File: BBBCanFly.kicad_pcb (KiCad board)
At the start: 2 copper layers, 86.4 x 54.7 mm, 26 parts, among them P1 CONN_01X02, P12 CONN_01X03, P13 CONN_01X03, P2 CONN_1x2, P3 CONN_02X23, P4 CONN_02X23, P5 CONN_02X05, P6 CONN_10, P7 CONN_4, P8 CONN_01X03, P9 CONN_01X03, U1 HT7465

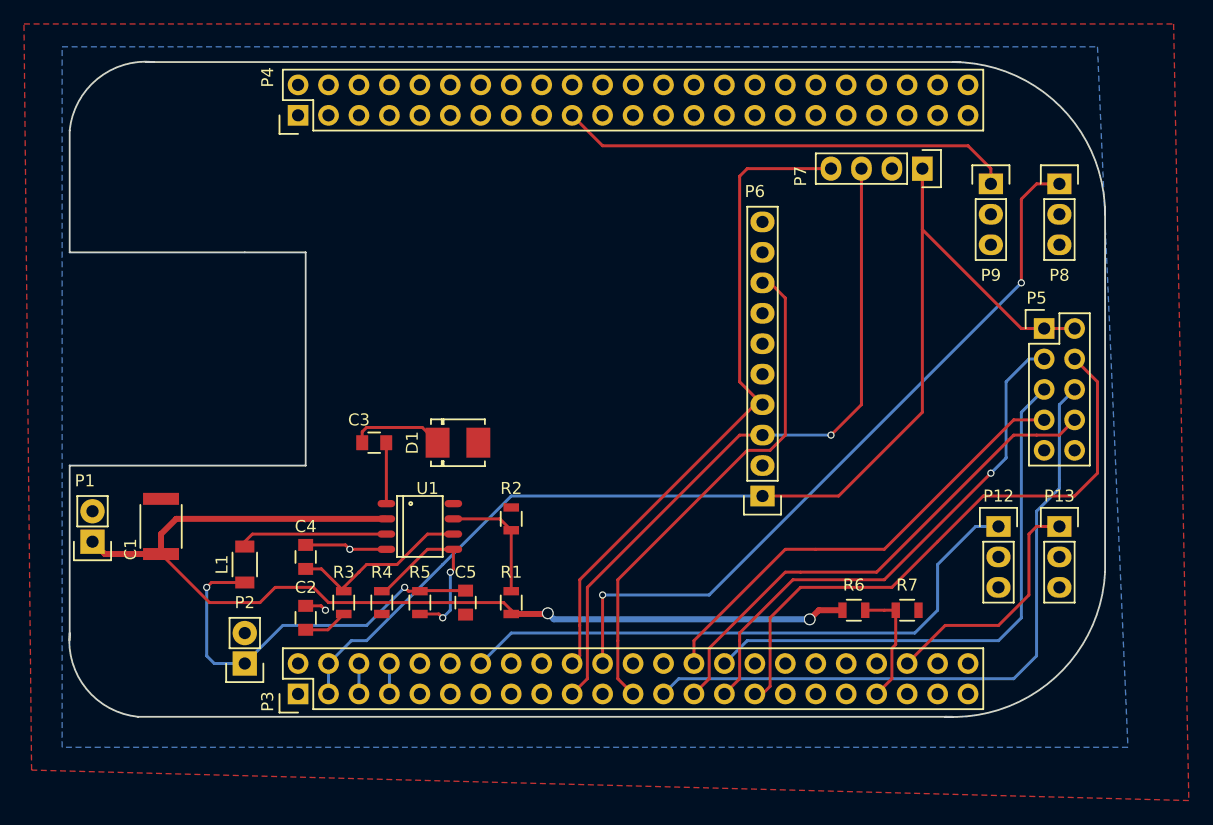
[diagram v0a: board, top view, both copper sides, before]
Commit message: modified power supply program
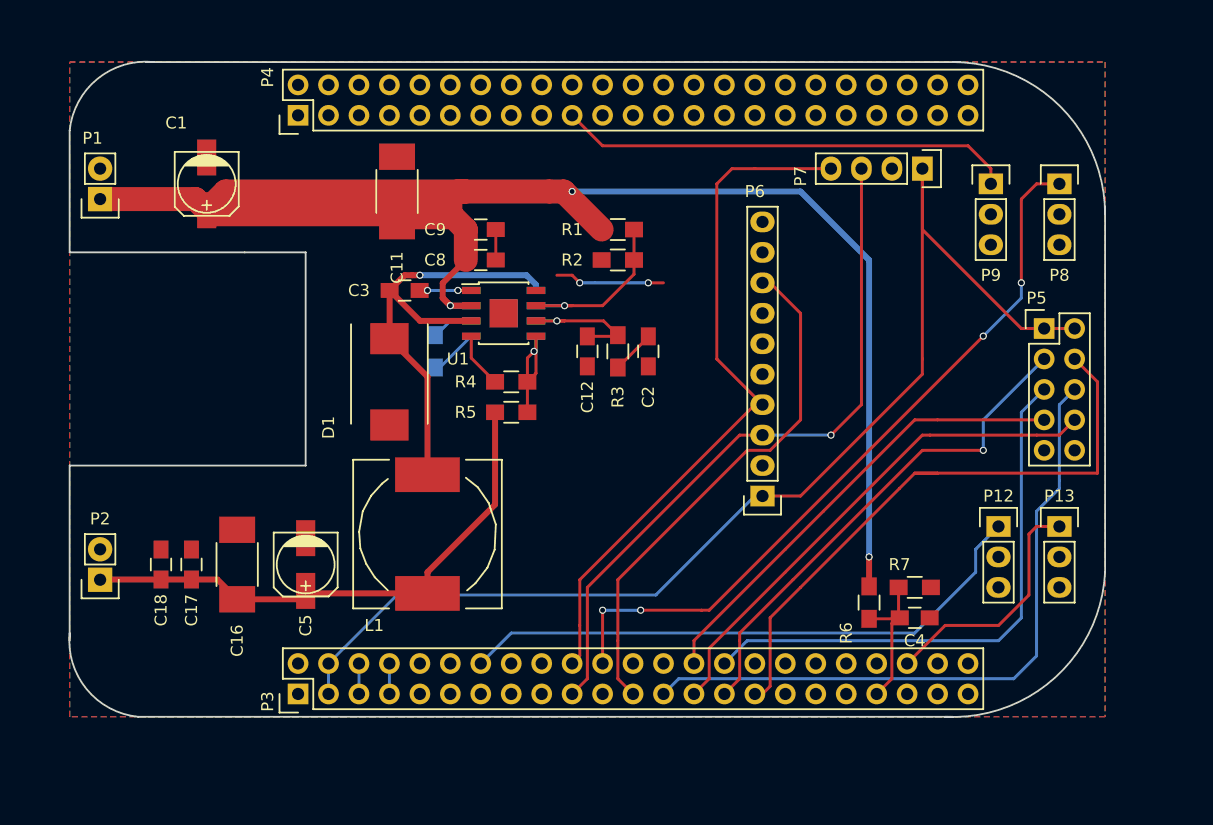
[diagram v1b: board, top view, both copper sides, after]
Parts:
- added C11: C, Capacitors_SMD:C_1812_HandSoldering, F.Cu at (52.7, 36.2)
- added C12: C, Capacitors_SMD:C_0805_HandSoldering, F.Cu at (68.6, 49.5)
- added C16: C, Capacitors_SMD:C_1812_HandSoldering, F.Cu at (39.4, 67.3)
- added C17: C, Capacitors_SMD:C_0805_HandSoldering, F.Cu at (35.6, 67.3)
- added C18: C, Capacitors_SMD:C_0805_HandSoldering, F.Cu at (33.0, 67.3)
- added C8: C, Capacitors_SMD:C_0805_HandSoldering, F.Cu at (59.7, 41.9)
- added C9: C, Capacitors_SMD:C_0805_HandSoldering, F.Cu at (59.7, 39.4)
- added R8: 200k, Resistors_SMD:R_0805_HandSoldering, B.Cu at (55.9, 49.5)
- added U2: MP1584EN, Housings_SOIC:SOIC-8-1EP_3.9x4.9mm_Pitch1.27mm, B.Cu at (61.6, 46.4)
- C1: footprint Capacitors_SMD:C_1812 -> Capacitors_SMD:c_elec_5x5.7
- C2, C3: footprint Capacitors_SMD:C_0805 -> Capacitors_SMD:C_0805_HandSoldering
- C4: value 1n -> 10p; footprint Capacitors_SMD:C_0805 -> Capacitors_SMD:C_0805_HandSoldering
- C5: footprint Capacitors_SMD:C_0805 -> Capacitors_SMD:c_elec_5x5.7
- D1: footprint Diodes_SMD:DO-214BA -> Diodes_SMD:DO-214AB
- L1: footprint Capacitors_SMD:C_1206 -> Inductors_NEOSID:Neosid_Inductor_SM-NE127
- R1: value 10k -> 100k; footprint Resistors_SMD:R_0805 -> Resistors_SMD:R_0805_HandSoldering
- R2, R3, R4, R6, R7: footprint Resistors_SMD:R_0805 -> Resistors_SMD:R_0805_HandSoldering
- R5: value 44.2k -> 47k; footprint Resistors_SMD:R_0805 -> Resistors_SMD:R_0805_HandSoldering
- U1: footprint Power_Integrations:SO-8 -> Housings_SOIC:SOIC-8-1EP_3.9x4.9mm_Pitch1.27mm
- moved C4 51.1 mm to (95.9, 71.8), turned to 0 degrees
- moved C2 36.2 mm to (73.7, 49.5), turned to 270 degrees
- moved R1 32.4 mm to (71.1, 39.4), turned to 0 degrees
- moved R3 31.0 mm to (71.1, 49.5)
- moved C1 28.8 mm to (36.8, 35.6), turned to 270 degrees
- moved P1 28.6 mm to (27.9, 36.8)
- moved R2 23.3 mm to (71.1, 41.9), turned to 180 degrees
- moved R4 21.3 mm to (62.2, 52.1), turned to 180 degrees
- moved U1 19.1 mm to (61.6, 46.4), turned to 0 degrees
- moved R5 17.6 mm to (62.2, 54.6), turned to 0 degrees
- moved L1 15.5 mm to (55.2, 64.8)
- moved P2 13.9 mm to (27.9, 68.6)
- moved C5 13.7 mm to (45.1, 67.3)
- moved C3 13.0 mm to (53.3, 44.5)
- moved D1 7.65 mm to (52.1, 52.1), turned to 270 degrees
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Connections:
- net +24V renamed /interface/24V
- net Net-(C3-Pad2) renamed /power/BST
- net Net-(C5-Pad1) renamed /power/output
- net Net-(R1-Pad2) renamed /power/EN
- net Net-(R4-Pad1) renamed /power/FB
- C3 pad 1: Net-(C3-Pad1) -> /power/SW
- C4 pad 1: Net-(C4-Pad1) -> /interface/AIN0
- D1 pad 1: Net-(C3-Pad1) -> /power/SW
- L1 pad 2: Net-(L1-Pad2) -> /power/SW
- P12 pad 2: Net-(P12-Pad2) -> (no net)
- P13 pad 2: Net-(P13-Pad2) -> (no net)
- P3 pad 10: /interface/SYS_RESETN -> (no net)
- P3 pad 11: /interface/UART4_RXD -> (no net)
- P3 pad 12: /interface/GPIO_60 -> (no net)
- P3 pad 13: /interface/UART4_TXD -> (no net)
- P3 pad 15: /interface/GPI0_48 -> (no net)
- P3 pad 16: /interface/EHRPWM1B -> (no net)
- P3 pad 17: /interface/SPI0_CS0 -> (no net)
- P3 pad 18: /interface/SPI0_D1 -> (no net)
- P3 pad 21: /interface/SPI0_DO -> (no net)
- P3 pad 24: /interface/UART1_TXD -> (no net)
- P3 pad 26: /interface/UART1_RXD -> (no net)
- P3 pad 32: /interface/VDD_ADC -> (no net)
- P3 pad 33: /interface/AIN4 -> (no net)
- P3 pad 34: /interface/GNDA_ADC -> (no net)
- P3 pad 35: /interface/AIN6 -> (no net)
- P3 pad 36: /interface/AIN5 -> (no net)
- P3 pad 37: /interface/AIN2 -> (no net)
- P3 pad 38: /interface/AIN3 -> (no net)
- P3 pad 40: /interface/AIN1 -> (no net)
- P3 pad 41: /interface/GPIO_20 -> (no net)
- P3 pad 9: /interface/PWR_BUT -> (no net)
- P4 pad 10: /interface/GPIO_68 -> (no net)
- P4 pad 11: /interface/GPIO_45 -> (no net)
- P4 pad 12: /interface/GPIO_44 -> (no net)
- P4 pad 13: /interface/EHPRWM2B -> (no net)
- P4 pad 14: /interface/GPIO_26 -> (no net)
- P4 pad 15: /interface/GPIO_47 -> (no net)
- P4 pad 16: /interface/GPIO_46 -> (no net)
- P4 pad 17: /interface/GPIO_27 -> (no net)
- P4 pad 18: /interface/GPIO_65 -> (no net)
- P4 pad 20: /interface/MMC1_CMD -> (no net)
- P4 pad 21: /interface/MMC1_CLK -> (no net)
- P4 pad 22: /interface/MMC1_DAT5 -> (no net)
- P4 pad 23: /interface/MMC1_DATA4 -> (no net)
- P4 pad 24: /interface/MMC1_DAT1 -> (no net)
- P4 pad 25: /interface/MMC1_DATA0 -> (no net)
- P4 pad 26: /interface/GPIO_61 -> (no net)
- P4 pad 27: /interface/LCD_VSYNC -> (no net)
- P4 pad 28: /interface/LCD_PLCK -> (no net)
- P4 pad 29: /interface/LCD_HSYNC -> (no net)
- P4 pad 3: /interface/MMC1_DATA6 -> (no net)
- P4 pad 30: /interface/LCD_AC_BIAS -> (no net)
- P4 pad 31: /interface/LCD_DATA14 -> (no net)
- P4 pad 32: /interface/LCD_DATA15 -> (no net)
- P4 pad 33: /interface/LCD_DATA13 -> (no net)
- P4 pad 34: /interface/LCD_DATA11 -> (no net)
- P4 pad 35: /interface/LCD_DATA12 -> (no net)
- P4 pad 36: /interface/LCD_DATA10 -> (no net)
- P4 pad 37: /interface/LCD_DATA8 -> (no net)
- P4 pad 38: /interface/LCD_DATA9 -> (no net)
- P4 pad 39: /interface/LCD_DATA6 -> (no net)
- P4 pad 4: /interface/MMC1_DAT7 -> (no net)
- P4 pad 40: /interface/LCD_DATA7 -> (no net)
- P4 pad 41: /interface/LCD_DATA4 -> (no net)
- P4 pad 42: /interface/LCD_DATA5 -> (no net)
- P4 pad 43: /interface/LCD_DATA2 -> (no net)
- P4 pad 44: /interface/LCD_DATA3 -> (no net)
- P4 pad 45: /interface/LCD_DATA0 -> (no net)
- P4 pad 46: /interface/LCD_DATA1 -> (no net)
- P4 pad 5: /interface/MMC1_DATA2 -> (no net)
- P4 pad 6: /interface/MMC1_DAT3 -> (no net)
- P4 pad 7: /interface/GPIO_66 -> (no net)
- P4 pad 8: /interface/GPIO_67 -> (no net)
- P4 pad 9: /interface/GPIO_69 -> (no net)
- P6 pad 5: /interface/EDA -> (no net)
- P6 pad 6: /interface/ECL -> (no net)
- P6 pad 7: /interface/ADO -> (no net)
- P6 pad 9: /interface/NCS -> (no net)
- P8 pad 2: Net-(P8-Pad2) -> (no net)
- P9 pad 2: Net-(P9-Pad2) -> (no net)
- R3 pad 1: Net-(C4-Pad1) -> /power/COMP
- U1 pad 3: Net-(L1-Pad2) -> /power/SW
- U1 pad 6: Net-(C4-Pad1) -> /power/COMP
- U1 pad 8: Net-(U1-Pad8) -> (no net)
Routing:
- net /interface/24V: track 87.8 -> 143.2 mm, vias 2 -> 3
- net /power/SW: track 0.00 -> 38.1 mm, vias 0 -> 1
- net Net-(C4-Pad1): track 15.3 -> 0.00 mm
- net /power/output: track 33.7 -> 46.9 mm, vias 2 -> 0
- net Net-(L1-Pad2): track 12.5 -> 0.00 mm
- net /power/COMP: track 0.00 -> 12.3 mm, vias 0 -> 1
- net (no net): track 0.00 -> 9.79 mm, vias 0 -> 2
- net Net-(C3-Pad1): track 7.87 -> 0.00 mm
- net /power/EN: track 10.3 -> 16.0 mm, vias 0 -> 1
- net /power/FB: track 15.5 -> 10.8 mm, vias 2 -> 1
- net Net-(R8-Pad1): track 0.00 -> 3.51 mm
- net GND: track 8.68 -> 11.4 mm, vias 2 -> 0
- net /interface/I2C2_SDA: track 56.3 -> 58.6 mm
- net /interface/SPI1_DO: track 44.2 -> 42.0 mm
- net /interface/AIN0: track 10.2 -> 12.2 mm
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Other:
- net class 24v: trace_width 0.5 -> 2
- net class output added: clearance 0.25, trace_width 0.5, via_dia 0.6, via_drill 0.4
